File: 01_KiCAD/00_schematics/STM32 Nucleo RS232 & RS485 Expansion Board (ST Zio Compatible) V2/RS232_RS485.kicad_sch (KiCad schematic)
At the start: 38 parts, among them J1 1190299, J2 CONN D-SUB PLUG 9POS TH, J3 HEADER 3POS 2.54mm, U2 THVD4431RHAR

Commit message: Finishing up the schematic aand created the board outline
Made some finishing touches to the schematic, updated all the symbol footprints and started to create the board.
Added missing 3D models for Phoenix 4-p RS485 connector and RS232 connector, also for Inolux LED.
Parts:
- J2: footprint (none) -> SubD-M-2301843-2:CONN9_2301843-2_TEC
- J3: value HEADER 3POS 2.54mm -> TCVR_PWR; footprint (none) -> HTSW-103-07-F-S:CON3_1X3_TU_TSW
- TP10, TP12, TP14, TP16, TP18, TP20, TP22, TP24: footprint 5008:KEYSTONE_5008 -> 5008_Orange:KEYSTONE_5008
- TP11, TP13, TP15, TP17, TP19, TP21, TP23, TP9: footprint 5009:KEYSTONE_5009 -> 5009_Yellow:KEYSTONE_5009
- TP25, TP26: footprint 5006:KEYSTONE_5006 -> 5006_Black:KEYSTONE_5006
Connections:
- net MCU_SHDN_N_1 renamed MCU_SHDN
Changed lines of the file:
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@@
 		)
 	)
-	(global_label "MCU_SHDN_N_1"
+	(global_label "MCU_SHDN"
 		(shape input)
 		(at 44.45 121.92 180)
@@
 		)
 		(property "Intersheetrefs" "${INTERSHEET_REFS}"
-			(at 26.8296 121.92 0)
+			(at 31.3048 121.92 0)
 			(effects
 				(font
@@
 	)
 	(symbol
-		(lib_name "5006_1")
 		(lib_id "5006_Black:5006")
 		(at 177.8 53.34 0)
@@
 			)
 		)
-		(property "Footprint" "5006:KEYSTONE_5006"
+		(property "Footprint" "5006_Black:KEYSTONE_5006"
 			(at 177.8 53.34 0)
 			(effects
@@
 	)
 	(symbol
-		(lib_name "5009_5")
 		(lib_id "5009_Yellow:5009")
 		(at 118.11 38.1 0)
@@
 			)
 		)
-		(property "Footprint" "5009:KEYSTONE_5009"
+		(property "Footprint" "5009_Yellow:KEYSTONE_5009"
 			(at 118.11 38.1 0)
 			(effects
@@
 			)
 		)
-		(property "Footprint" "5008:KEYSTONE_5008"
+		(property "Footprint" "5008_Orange:KEYSTONE_5008"
 			(at 177.8 45.72 0)
 			(effects
@@
 			)
 		)
-		(property "Footprint" "5008:KEYSTONE_5008"
+		(property "Footprint" "5008_Orange:KEYSTONE_5008"
 			(at 177.8 38.1 0)
 			(effects
@@
 		(dnp no)
 		(fields_autoplaced yes)
-		(property "Reference" "#PWR067"
+		(property "Reference" "#PWR018"
 			(at 187.96 59.69 0)
 			(effects
@@
 			(project "STM32 Nucleo RS232 & RS485 Expansion Board (ST Zio Compatible) V2"
 				(path "/080f83b7-8913-48e8-ab8e-79cb12295542/eb278bca-04f9-4d71-99cd-ac1b982e4a86"
-					(reference "#PWR067")
+					(reference "#PWR018")
 					(unit 1)
 				)
@@
 		(dnp no)
 		(fields_autoplaced yes)
-		(property "Reference" "#PWR021"
+		(property "Reference" "#PWR023"
 			(at 119.38 95.25 0)
 			(effects
@@
 			(project "STM32 Nucleo RS232 & RS485 Expansion Board (ST Zio Compatible) V2"
 				(path "/080f83b7-8913-48e8-ab8e-79cb12295542/eb278bca-04f9-4d71-99cd-ac1b982e4a86"
-					(reference "#PWR021")
+					(reference "#PWR023")
 					(unit 1)
 				)
@@
 			)
 		)
-		(property "Footprint" "5008:KEYSTONE_5008"
+		(property "Footprint" "5008_Orange:KEYSTONE_5008"
 			(at 177.8 41.91 0)
 			(effects
@@
 		(dnp no)
 		(fields_autoplaced yes)
-		(property "Reference" "#PWR024"
+		(property "Reference" "#PWR026"
 			(at 118.11 152.4 0)
 			(effects
@@
 			(project "STM32 Nucleo RS232 & RS485 Expansion Board (ST Zio Compatible) V2"
 				(path "/080f83b7-8913-48e8-ab8e-79cb12295542/eb278bca-04f9-4d71-99cd-ac1b982e4a86"
-					(reference "#PWR024")
+					(reference "#PWR026")
 					(unit 1)
 				)
@@
 	)
 	(symbol
-		(lib_name "5009_1")
 		(lib_id "5009_Yellow:5009")
 		(at 118.11 22.86 0)
@@
 			)
 		)
-		(property "Footprint" "5009:KEYSTONE_5009"
+		(property "Footprint" "5009_Yellow:KEYSTONE_5009"
 			(at 118.11 22.86 0)
 			(effects
@@
 			)
 		)
-		(property "Footprint" "5006:KEYSTONE_5006"
+		(property "Footprint" "5006_Black:KEYSTONE_5006"
 			(at 118.11 53.34 0)
 			(effects
@@
 		(dnp no)
 		(fields_autoplaced yes)
-		(property "Reference" "#PWR019"
+		(property "Reference" "#PWR021"
 			(at 85.09 95.25 0)
 			(effects
@@
 			(project "STM32 Nucleo RS232 & RS485 Expansion Board (ST Zio Compatible) V2"
 				(path "/080f83b7-8913-48e8-ab8e-79cb12295542/eb278bca-04f9-4d71-99cd-ac1b982e4a86"
-					(reference "#PWR019")
+					(reference "#PWR021")
 					(unit 1)
 				)
@@
 		(dnp no)
 		(fields_autoplaced yes)
-		(property "Reference" "#PWR066"
+		(property "Reference" "#PWR017"
 			(at 107.95 59.69 0)
 			(effects
@@
 			(project "STM32 Nucleo RS232 & RS485 Expansion Board (ST Zio Compatible) V2"
 				(path "/080f83b7-8913-48e8-ab8e-79cb12295542/eb278bca-04f9-4d71-99cd-ac1b982e4a86"
-					(reference "#PWR066")
+					(reference "#PWR017")
 					(unit 1)
 				)
@@
 	)
 	(symbol
-		(lib_name "5009_4")
 		(lib_id "5009_Yellow:5009")
 		(at 118.11 34.29 0)
@@
 			)
 		)
-		(property "Footprint" "5009:KEYSTONE_5009"
+		(property "Footprint" "5009_Yellow:KEYSTONE_5009"
 			(at 118.11 34.29 0)
 			(effects
@@
 		(dnp no)
 		(fields_autoplaced yes)
-		(property "Reference" "#PWR020"
+		(property "Reference" "#PWR022"
 			(at 102.87 95.25 0)
 			(effects
@@
 			(project "STM32 Nucleo RS232 & RS485 Expansion Board (ST Zio Compatible) V2"
 				(path "/080f83b7-8913-48e8-ab8e-79cb12295542/eb278bca-04f9-4d71-99cd-ac1b982e4a86"
-					(reference "#PWR020")
+					(reference "#PWR022")
 					(unit 1)
 				)
@@
 		(dnp no)
 		(fields_autoplaced yes)
-		(property "Reference" "#PWR023"
+		(property "Reference" "#PWR025"
 			(at 93.98 152.4 0)
 			(effects
@@
 			(project "STM32 Nucleo RS232 & RS485 Expansion Board (ST Zio Compatible) V2"
 				(path "/080f83b7-8913-48e8-ab8e-79cb12295542/eb278bca-04f9-4d71-99cd-ac1b982e4a86"
-					(reference "#PWR023")
+					(reference "#PWR025")
 					(unit 1)
 				)
@@
 		(dnp no)
 		(fields_autoplaced yes)
-		(property "Reference" "#PWR026"
+		(property "Reference" "#PWR028"
 			(at 213.36 152.4 0)
 			(effects
@@
 			(project "STM32 Nucleo RS232 & RS485 Expansion Board (ST Zio Compatible) V2"
 				(path "/080f83b7-8913-48e8-ab8e-79cb12295542/eb278bca-04f9-4d71-99cd-ac1b982e4a86"
-					(reference "#PWR026")
+					(reference "#PWR028")
 					(unit 1)
 				)
@@
 	)
 	(symbol
-		(lib_name "5009_7")
 		(lib_id "5009_Yellow:5009")
 		(at 118.11 45.72 0)
@@
 			)
 		)
-		(property "Footprint" "5009:KEYSTONE_5009"
+		(property "Footprint" "5009_Yellow:KEYSTONE_5009"
 			(at 118.11 45.72 0)
 			(effects
@@
 		(dnp no)
 		(fields_autoplaced yes)
-		(property "Reference" "#PWR025"
+		(property "Reference" "#PWR027"
 			(at 138.43 152.4 0)
 			(effects
@@
 			(project "STM32 Nucleo RS232 & RS485 Expansion Board (ST Zio Compatible) V2"
 				(path "/080f83b7-8913-48e8-ab8e-79cb12295542/eb278bca-04f9-4d71-99cd-ac1b982e4a86"
-					(reference "#PWR025")
+					(reference "#PWR027")
 					(unit 1)
 				)
@@
 			)
 		)
-		(property "Footprint" "5009:KEYSTONE_5009"
+		(property "Footprint" "5009_Yellow:KEYSTONE_5009"
 			(at 118.11 49.53 0)
 			(effects
@@
 		(dnp no)
 		(fields_autoplaced yes)
-		(property "Reference" "#PWR022"
+		(property "Reference" "#PWR024"
 			(at 262.89 129.54 0)
 			(effects
@@
 			(project ""
 				(path "/080f83b7-8913-48e8-ab8e-79cb12295542/eb278bca-04f9-4d71-99cd-ac1b982e4a86"
-					(reference "#PWR022")
+					(reference "#PWR024")
 					(unit 1)
 				)
@@
 			)
 		)
-		(property "Footprint" "5008:KEYSTONE_5008"
+		(property "Footprint" "5008_Orange:KEYSTONE_5008"
 			(at 177.8 26.67 0)
 			(effects
@@
 			)
 		)
-		(property "Footprint" ""
+		(property "Footprint" "SubD-M-2301843-2:CONN9_2301843-2_TEC"
 			(at 273.05 106.68 0)
 			(effects
@@
 			)
 		)
-		(property "Datasheet" "https://www.lcsc.com/datasheet/C591554.pdf"
+		(property "Datasheet" "~"
 			(at 273.05 106.68 0)
 			(effects
@@
 			)
 		)
-		(property "Description" "Connector D-Sub, Male 9 Position 2 Row Through Hole"
+		(property "Description" "9-pin D-SUB connector, pins (male)"
 			(at 273.05 106.68 0)
 			(effects
@@
 		(dnp no)
 		(fields_autoplaced yes)
-		(property "Reference" "#PWR018"
+		(property "Reference" "#PWR020"
 			(at 69.85 95.25 0)
 			(effects
@@
 			(project "STM32 Nucleo RS232 & RS485 Expansion Board (ST Zio Compatible) V2"
 				(path "/080f83b7-8913-48e8-ab8e-79cb12295542/eb278bca-04f9-4d71-99cd-ac1b982e4a86"
-					(reference "#PWR018")
+					(reference "#PWR020")
 					(unit 1)
 				)
@@
 			)
 		)
-		(property "Footprint" "5008:KEYSTONE_5008"
+		(property "Footprint" "5008_Orange:KEYSTONE_5008"
 			(at 177.8 22.86 0)
 			(effects
@@
 			)
 		)
-		(property "Value" "HEADER 3POS 2.54mm"
-			(at 41.656 135.89 90)
+		(property "Value" "TCVR_PWR"
+			(at 54.102 136.144 90)
 			(effects
 				(font
@@
 			)
 		)
-		(property "Footprint" ""
+		(property "Footprint" "HTSW-103-07-F-S:CON3_1X3_TU_TSW"
 			(at 68.58 135.89 0)
 			(effects
@@
 			)
 		)
-		(property "Datasheet" "https://www.lcsc.com/datasheet/C6631883.pdf"
+		(property "Datasheet" "~"
 			(at 68.58 135.89 0)
 			(effects
@@
 			)
 		)
-		(property "Description" "Pin Header 3 Position 2.54mm Pitch Single Row Through Hole -55℃~+125℃"
+		(property "Description" "Generic connector, single row, 01x03, script generated (kicad-library-utils/schlib/autogen/connector/)"
 			(at 68.58 135.89 0)
 			(effects
@@
 			)
 		)
-		(property "Footprint" "5008:KEYSTONE_5008"
+		(property "Footprint" "5008_Orange:KEYSTONE_5008"
 			(at 177.8 30.48 0)
 			(effects
@@
 	)
 	(symbol
-		(lib_name "5009_6")
 		(lib_id "5009_Yellow:5009")
 		(at 118.11 41.91 0)
@@
 			)
 		)
-		(property "Footprint" "5009:KEYSTONE_5009"
+		(property "Footprint" "5009_Yellow:KEYSTONE_5009"
 			(at 118.11 41.91 0)
 			(effects
@@
 			)
 		)
-		(property "Footprint" "5008:KEYSTONE_5008"
+		(property "Footprint" "5008_Orange:KEYSTONE_5008"
 			(at 177.8 34.29 0)
 			(effects
@@
 	)
 	(symbol
-		(lib_name "5009_3")
 		(lib_id "5009_Yellow:5009")
 		(at 118.11 30.48 0)
@@
 			)
 		)
-		(property "Footprint" "5009:KEYSTONE_5009"
+		(property "Footprint" "5009_Yellow:KEYSTONE_5009"
 			(at 118.11 30.48 0)
 			(effects
@@
 			)
 		)
-		(property "Footprint" "5008:KEYSTONE_5008"
+		(property "Footprint" "5008_Orange:KEYSTONE_5008"
 			(at 177.8 49.53 0)
 			(effects
@@
 	)
 	(symbol
-		(lib_name "5009_2")
 		(lib_id "5009_Yellow:5009")
 		(at 118.11 26.67 0)
@@
 			)
 		)
-		(property "Footprint" "5009:KEYSTONE_5009"
+		(property "Footprint" "5009_Yellow:KEYSTONE_5009"
 			(at 118.11 26.67 0)
 			(effects
@@
 		(dnp no)
 		(fields_autoplaced yes)
-		(property "Reference" "#PWR017"
+		(property "Reference" "#PWR019"
 			(at 54.61 95.25 0)
 			(effects
@@
 			(project "STM32 Nucleo RS232 & RS485 Expansion Board (ST Zio Compatible) V2"
 				(path "/080f83b7-8913-48e8-ab8e-79cb12295542/eb278bca-04f9-4d71-99cd-ac1b982e4a86"
-					(reference "#PWR017")
+					(reference "#PWR019")
 					(unit 1)
 				)

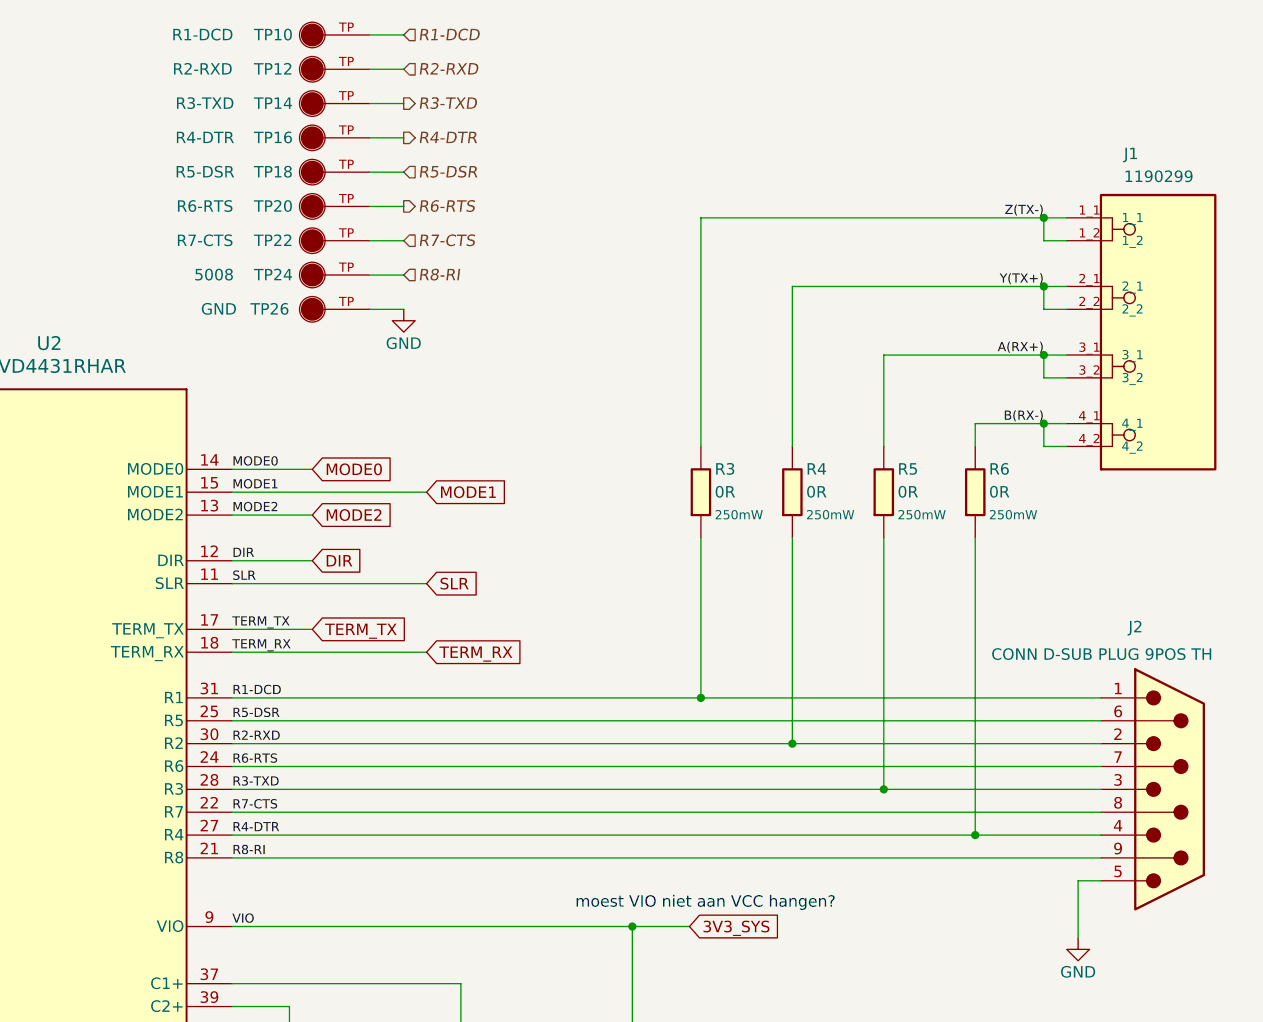
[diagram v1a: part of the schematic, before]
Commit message: Corrected RS485 connector layout
Corrected the layout and connections to Phoenix Contacts connector J1 so pairs are next to eachother and simplyfied the board layout to better match the THVD4431 connections.
Added some 3D models to the testpoints TP10, TP12, TP14 and TP16. Made color-coding for the RS485 pairs so they are easily identified as pairs belong to eachother.
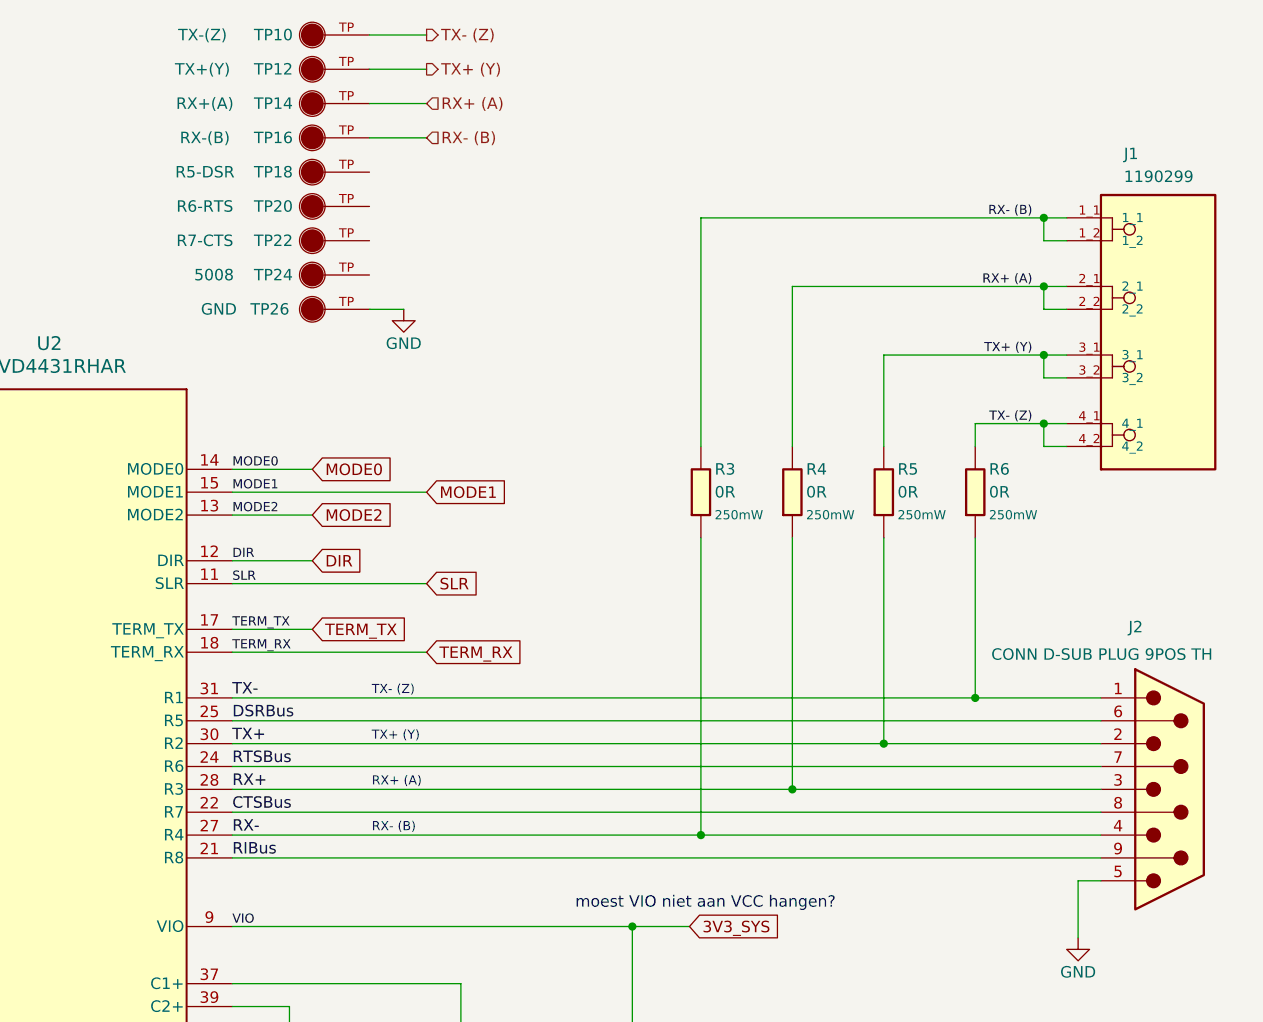
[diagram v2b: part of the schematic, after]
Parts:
- TP10: value R1-DCD -> TX-(Z)
- TP12: value R2-RXD -> TX+(Y)
- TP14: value R3-TXD -> RX+(A)
- TP16: value R4-DTR -> RX-(B)
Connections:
- net A(RX+) renamed TX+ (Y)
- net TX+ (Y): now also TP12.TP
- net B(RX-) renamed TX- (Z)
- net TX- (Z): now also TP10.TP
- net R1-DCD renamed TX-
- net TX-: now also R6.2; no longer R3.2, TP10.TP
- net R2-RXD renamed TX+
- net TX+: now also R5.2; no longer R4.2, TP12.TP
- net R3-TXD renamed RX+
- net RX+: now also R4.2; no longer R5.2, TP14.TP
- net R4-DTR renamed RX-
- net RX-: now also R3.2; no longer R6.2, TP16.TP
- net R5-DSR renamed DSRBus
- net DSRBus: no longer TP18.TP
- net R6-RTS renamed RTSBus
- net RTSBus: no longer TP20.TP
- net R7-CTS renamed CTSBus
- net CTSBus: no longer TP22.TP
- net R8-RI renamed RIBus
- net RIBus: no longer TP24.TP
- net Y(TX+) renamed RX+ (A)
- net RX+ (A): now also TP14.TP
- net Z(TX-) renamed RX- (B)
- net RX- (B): now also TP16.TP
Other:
- note added: "RX+ (A)"
- note added: "RX- (B)"
- note added: "TX+ (Y)"
- note added: "TX- (Z)"

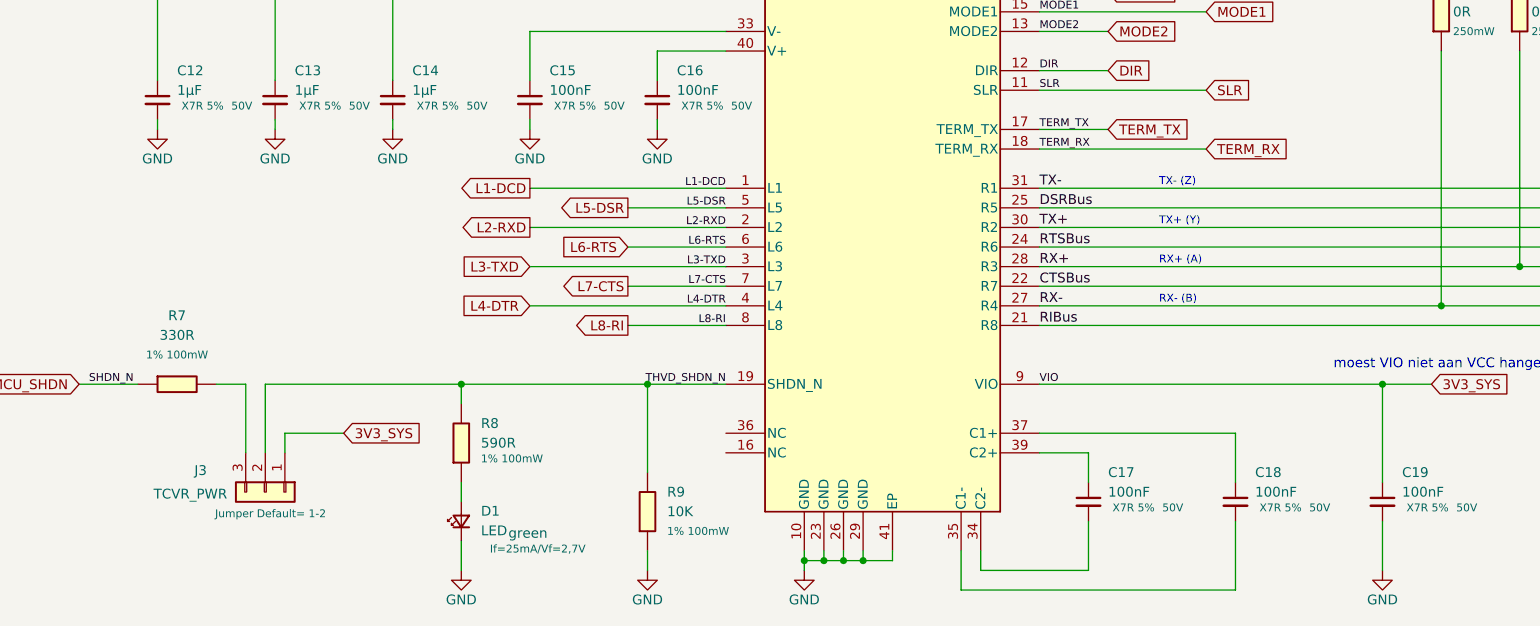
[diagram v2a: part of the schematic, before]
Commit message: Updated footprints and added components to PCB
Added some additional components to the board. Changed the footprint of the 3-pin Jumper so the bottom silkscreen text doesnlt overlap with the Dual Schmidt Trigger IC's SN74LVC2G14
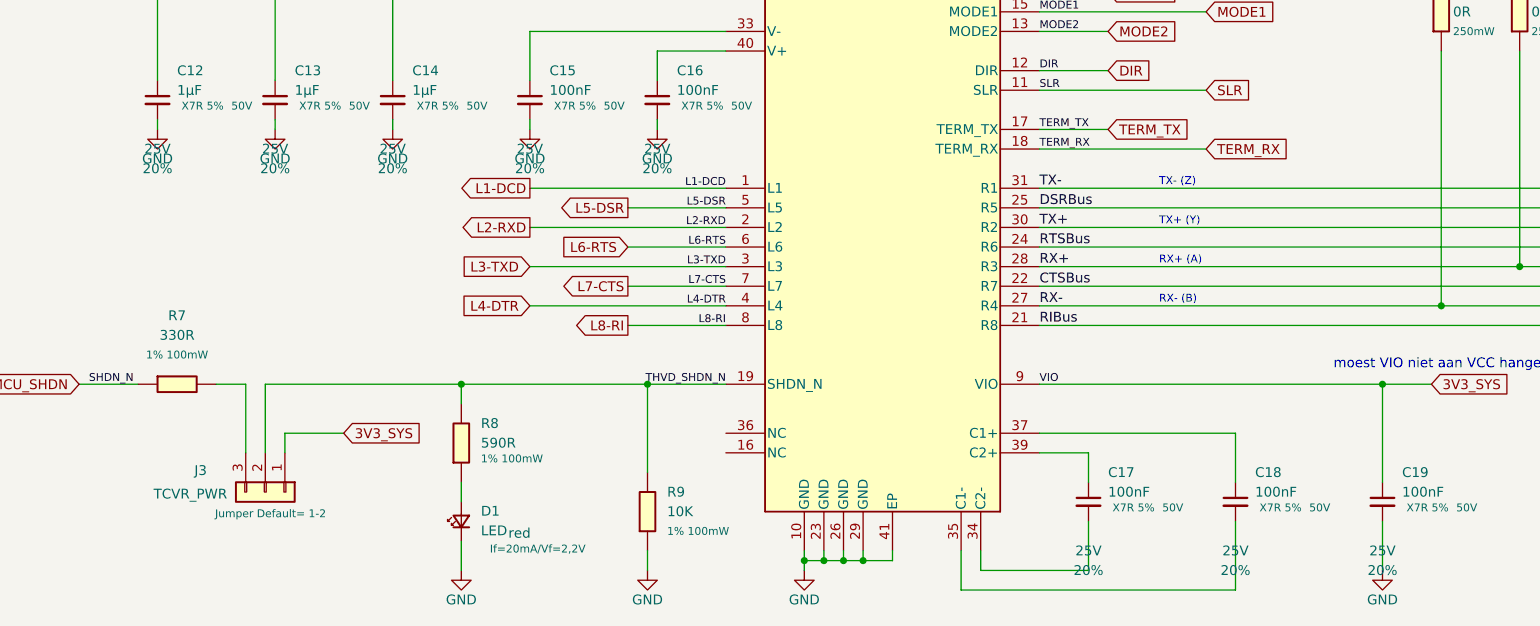
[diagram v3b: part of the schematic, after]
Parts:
- C12, C13, C14, C15, C16, C17, C18, C19: PROD_ID (none) -> CAP-00810; Tolerance (none) -> 20%; Voltage (none) -> 25V
- D1: Color green -> red; LCSC C5656662 -> C7286681; MPN IN-S63AT5G -> HSMZ-C190; Manufacturer Inolux -> Broadcom; Voltage Rating If=25mA/Vf=2,7V -> If=20mA/Vf=2,2V
- J3: footprint HTSW-103-07-F-S:CON3_1X3_TU_TSW -> Samtec_Connector:Samtec HTSW-103-07-F-S
